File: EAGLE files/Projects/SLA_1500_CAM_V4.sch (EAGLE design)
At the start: 91 parts, among them J2 JST GH SM06B, J3 MOLEX 53261-03, J4 MOLEX 53261-04, J5 MOLEX 53261-04, J6 MOLEX 53261-04, U11 TXS0102, U2 TPS73633DCQR, U8 TXS0102, U9 TXS0102

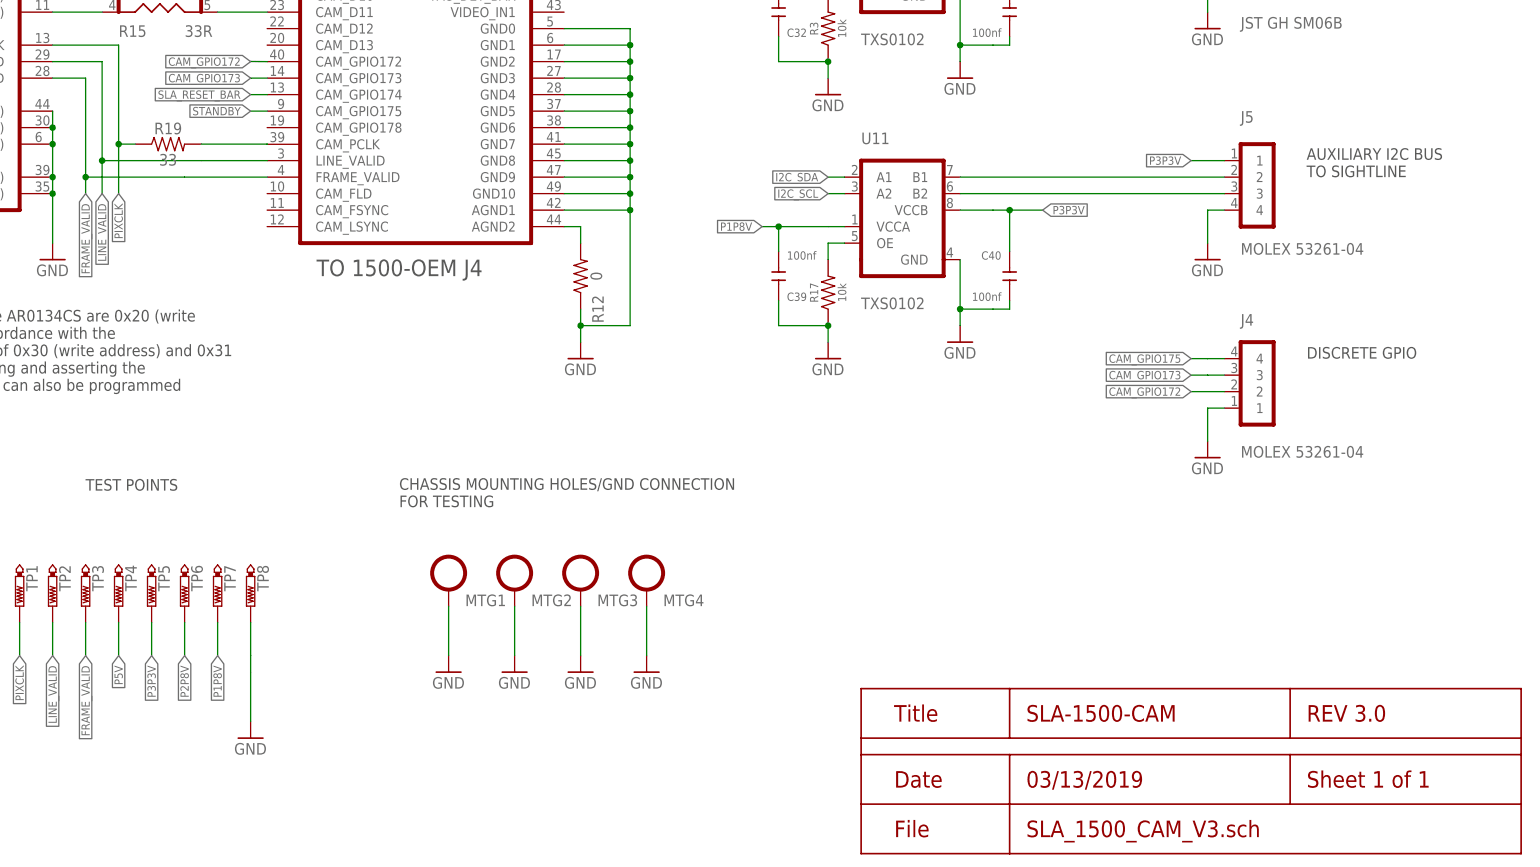
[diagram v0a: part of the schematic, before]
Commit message: Update SLA1500 CAM V4
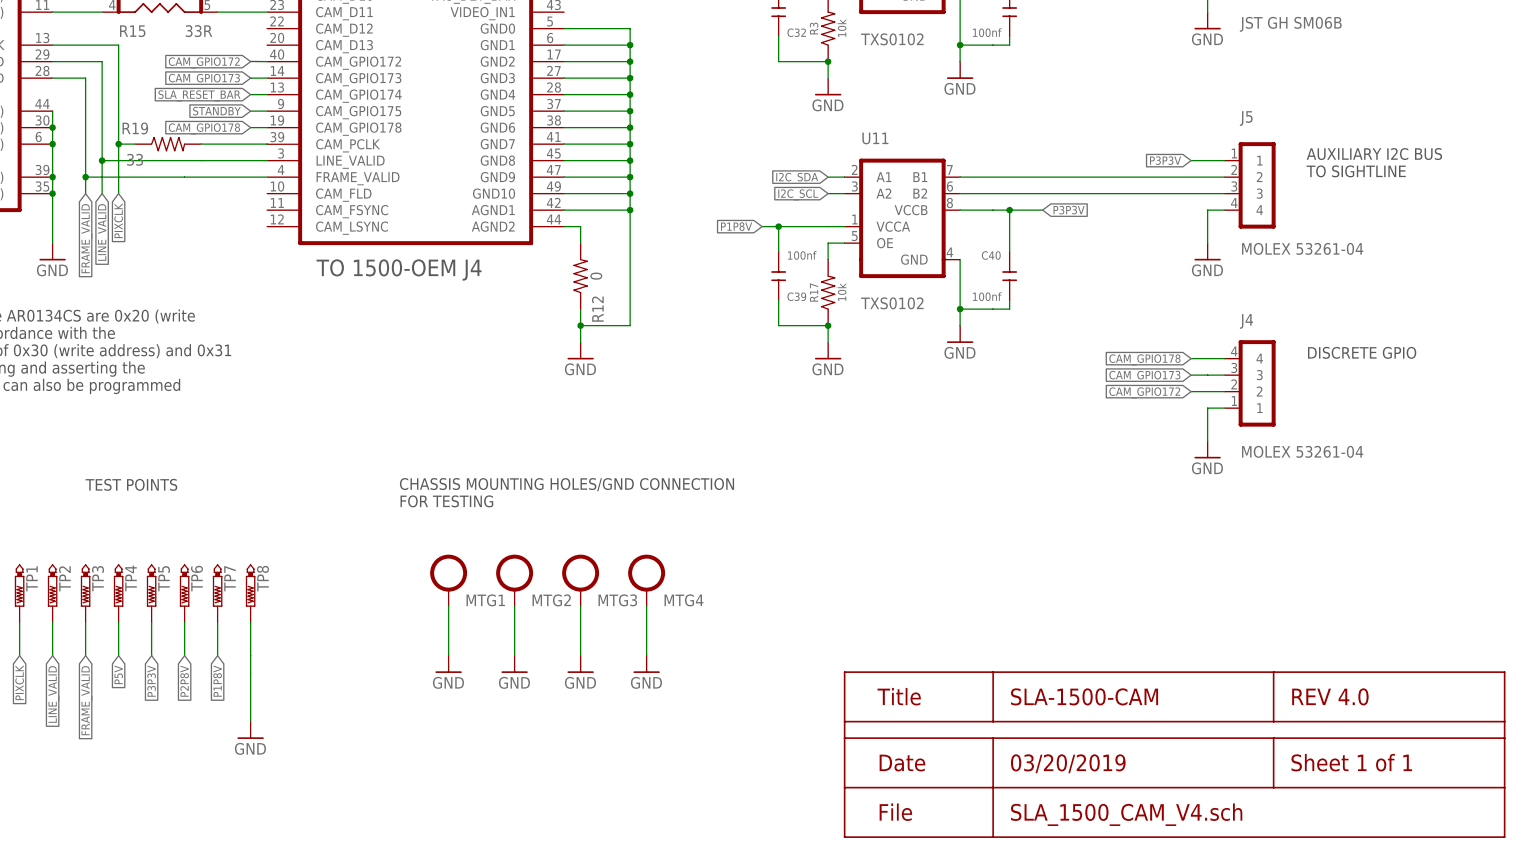
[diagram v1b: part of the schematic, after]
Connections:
- removed net CAM_GPIO175: J4.4
- new net CAM_GPIO178: J1.CAM_GPIO178, J4.4
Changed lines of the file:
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@@
 <part name="C15" library="Sightline" deviceset="CAP0201" device="100NF" package3d_urn="urn:adsk.eagle:package:26117/2"/>
 <part name="C16" library="Sightline" deviceset="CAP0201" device="100NF" package3d_urn="urn:adsk.eagle:package:26117/2"/>
-<part name="U$1" library="Sightline" deviceset="HEADER_V3" device=""/>
 <part name="C6" library="Seeed-Capacitor" library_urn="urn:adsk.eagle:library:464" deviceset="CERAMIC-100NF-25V-10%-X7R(0402)" device="" package3d_urn="urn:adsk.eagle:package:32379/1" value="100nf"/>
 <part name="C17" library="Seeed-Capacitor" library_urn="urn:adsk.eagle:library:464" deviceset="CERAMIC-100NF-25V-10%-X7R(0402)" device="" package3d_urn="urn:adsk.eagle:package:32379/1" value="100nf"/>
@@
 <part name="D2" library="diode" library_urn="urn:adsk.eagle:library:210" deviceset="BAT60J" device="" package3d_urn="urn:adsk.eagle:package:43461/1"/>
 <part name="D1" library="diode" library_urn="urn:adsk.eagle:library:210" deviceset="BAT60J" device="" package3d_urn="urn:adsk.eagle:package:43461/1"/>
+<part name="U$1" library="Sightline" deviceset="HEADER_V4" device=""/>
 </parts>
 <sheets>
@@
 <attribute name="NAME" x="54.61" y="62.23" size="1.27" layer="95"/>
 </instance>
-<instance part="U$1" gate="G$1" x="325.12" y="2.54" smashed="yes"/>
 <instance part="C6" gate="G$1" x="312.42" y="193.04" smashed="yes" rot="R90">
 <attribute name="NAME" x="313.69" y="189.23" size="1.27" layer="95" ratio="10" rot="R180" align="top-right"/>
@@
 </instance>
 <instance part="R19" gate="G$1" x="218.44" y="111.76" smashed="yes">
-<attribute name="NAME" x="218.44" y="113.284" size="1.778" layer="95" font="vector" align="bottom-center"/>
-<attribute name="VALUE" x="218.44" y="110.236" size="1.778" layer="96" font="vector" align="top-center"/>
+<attribute name="NAME" x="213.36" y="113.284" size="1.778" layer="95" font="vector" align="bottom-center"/>
+<attribute name="VALUE" x="213.36" y="110.236" size="1.778" layer="96" font="vector" align="top-center"/>
 </instance>
 <instance part="R20" gate="G$1" x="124.46" y="152.4" smashed="yes" rot="R90">
@@
 <attribute name="VALUE" x="366.649" y="152.654" size="1.778" layer="96" rot="R90"/>
 </instance>
+<instance part="U$1" gate="G$1" x="322.58" y="5.08" smashed="yes"/>
 </instances>
 <busses>
@@
 </segment>
 </net>
-<net name="CAM_GPIO175" class="0">
-<segment>
-<wire x1="381" y1="78.74" x2="378.46" y2="78.74" width="0.1524" layer="91"/>
-<label x="375.92" y="78.74" size="1.27" layer="97" rot="R180" xref="yes"/>
-<wire x1="378.46" y1="78.74" x2="375.92" y2="78.74" width="0.1524" layer="91"/>
-<pinref part="J4" gate="G$1" pin="4"/>
-</segment>
-</net>
 <net name="P5V" class="0">
 <segment>
@@
 </segment>
 </net>
+<net name="CAM_GPIO178" class="0">
+<segment>
+<pinref part="J4" gate="G$1" pin="4"/>
+<wire x1="381" y1="78.74" x2="375.92" y2="78.74" width="0.1524" layer="91"/>
+<label x="375.92" y="78.74" size="1.27" layer="95" rot="R180" xref="yes"/>
+</segment>
+<segment>
+<pinref part="J1" gate="G$1" pin="CAM_GPIO178"/>
+<wire x1="233.68" y1="114.3" x2="231.14" y2="114.3" width="0.1524" layer="91"/>
+<label x="231.14" y="114.3" size="1.27" layer="95" rot="R180" xref="yes"/>
+</segment>
+</net>
